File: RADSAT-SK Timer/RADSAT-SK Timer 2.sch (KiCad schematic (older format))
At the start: 52 parts, among them J201 Conn_01x07, J202 Conn_01x05, J203 Conn_01x03, J204 Conn_01x02, J205 Conn_01x02, J206 Conn_01x02, J210 ZX62WRD-B-5PC, Q201 IRLML2060, Q202 IRLML2060, Q204 IRLML2060, Q205 IRLML2060, Q206 IRLML2060, SW201 SW_Push, SW202 SW_Push, SW203 SW_Push, SW204 SW_Push, SW205 SW_Push, SW206 SW_Push, U202 LTC3440EMSPBF, U230 CPC1117N, U240 CPC1117N, U250 CPC1117N, U260 CPC1117N

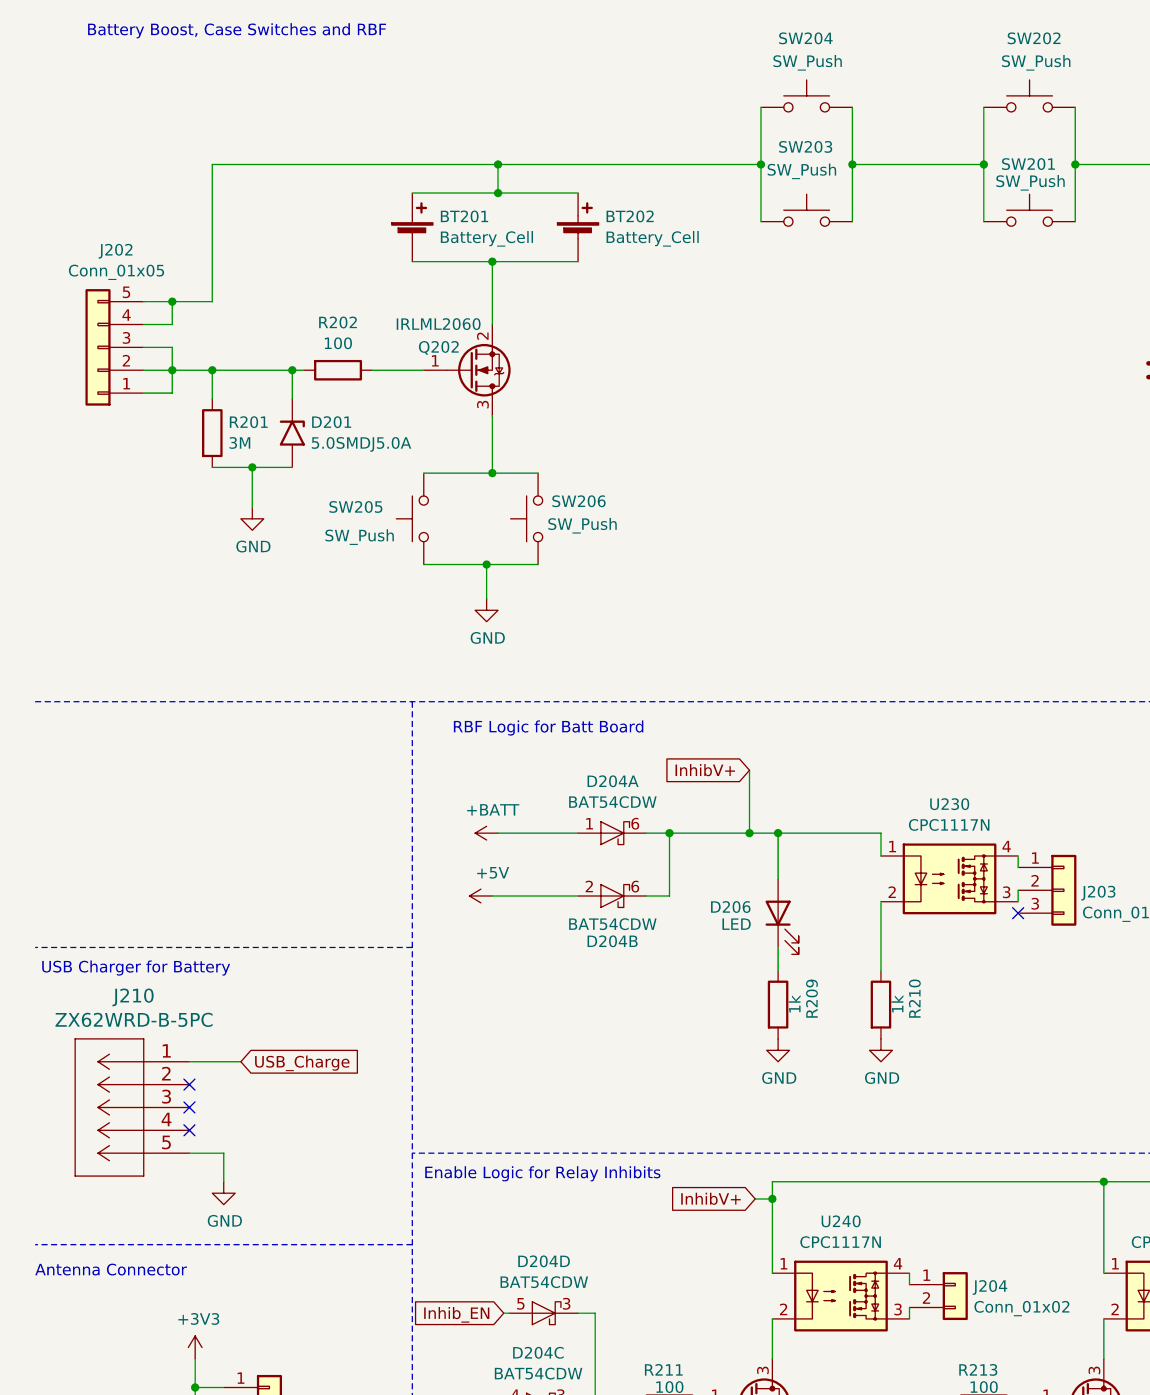
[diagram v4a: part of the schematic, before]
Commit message: Made changes to accomadate the RBF alternate charge plug
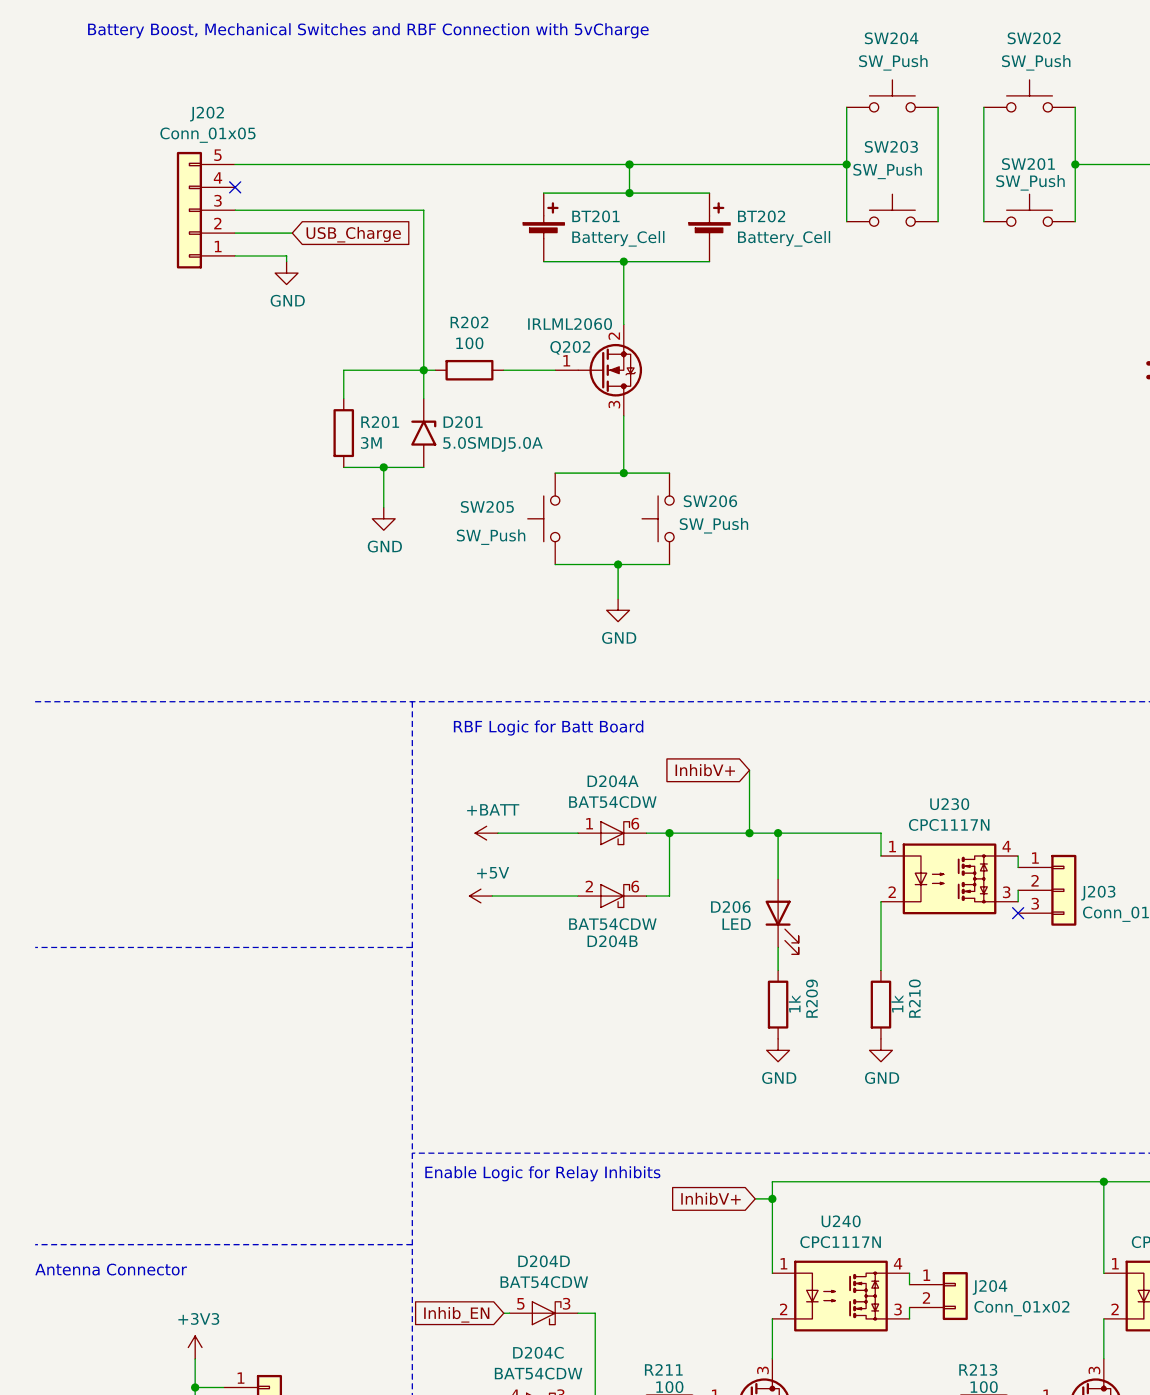
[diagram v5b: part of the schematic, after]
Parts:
- removed J210: ZX62WRD-B-5PC, CONN_ZX62WRD-B-5PC_HIR:CONN_ZX62WRD-B-5PC_HIR, symbol CONN_ZX62WRD-B-5PC_HIR:ZX62WRD-B-5PC
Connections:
- net GND: now also J202.1 (Pin_1)
- net USB_Charge: now also J202.2 (Pin_2)
- net at BT201.1 (+), BT202.1 (+), J202.5 (Pin_5)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: no longer J202.4 (Pin_4)
- net at SW203.2, SW204.2: no longer SW201.1, SW202.1
- net at D201.1 (A1), J202.3 (Pin_3), R201.1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: no longer J202.1 (Pin_1), J202.2 (Pin_2)
- new net: SW201.1, SW202.1
- no-connect marks 5 -> 3
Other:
- note added: "Battery Boost, Mechanical Switches and RBF Connection with 5vCharge"
- note removed: "Battery Boost, Case Switches and RBF"
- note removed: "USB Charger for Battery"
- moved on the sheet: BT201, BT202, D201, J202, Q202, R201, R202, SW203, SW204, SW205, SW206

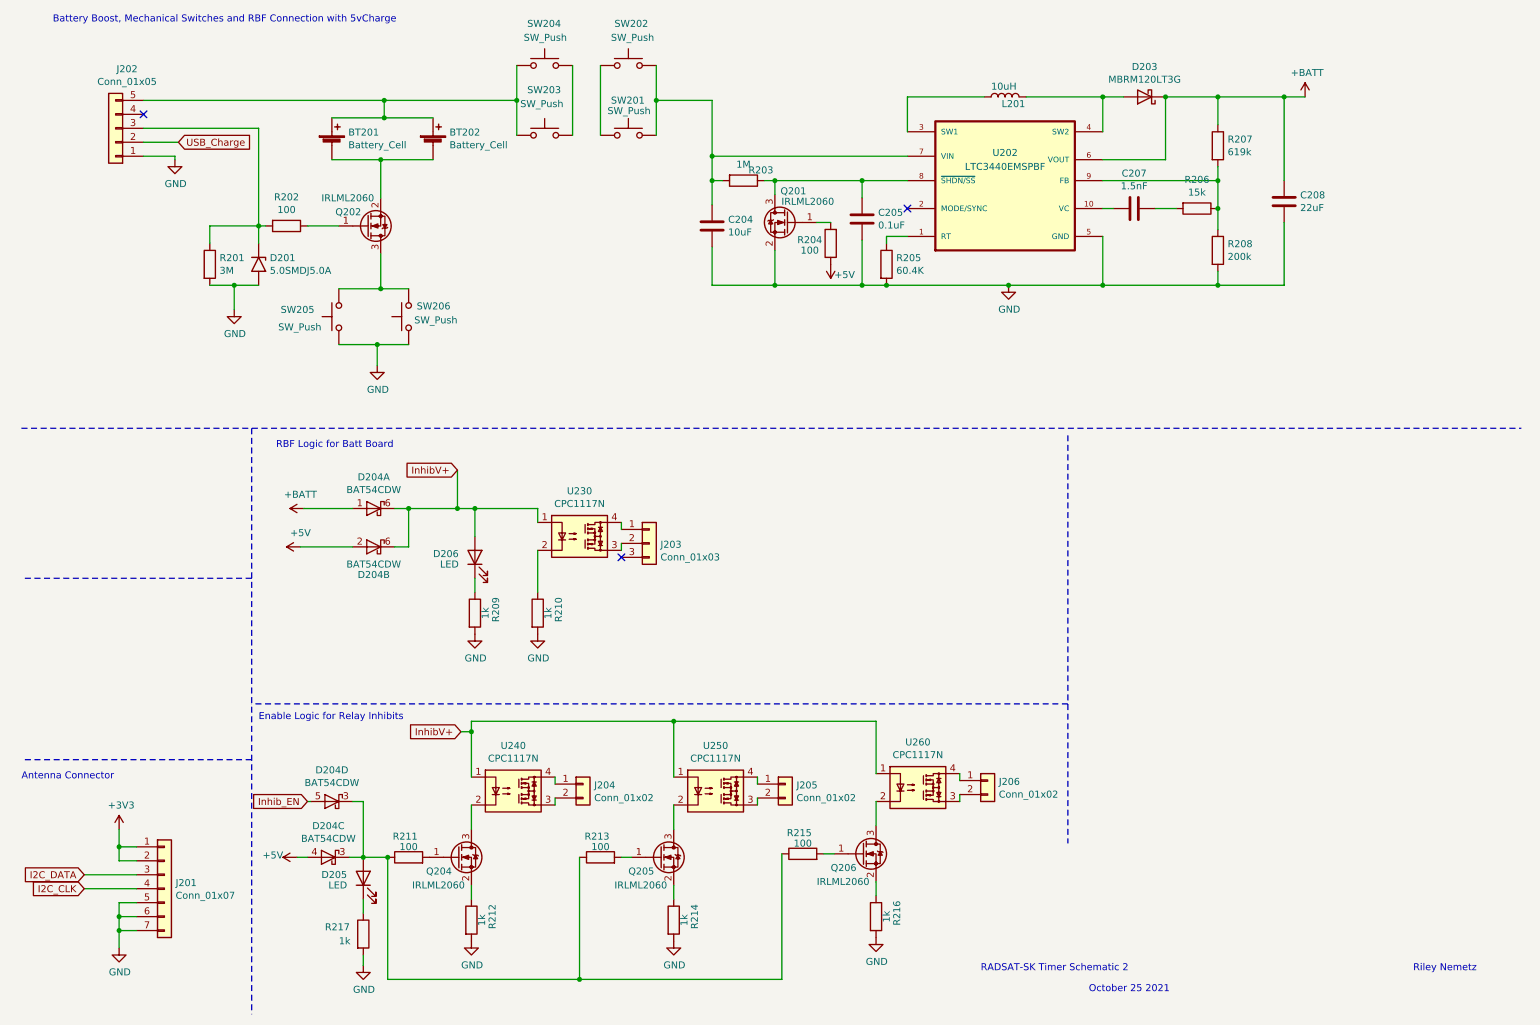
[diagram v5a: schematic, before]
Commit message: RBF Circuit was modified and new components added to BOM
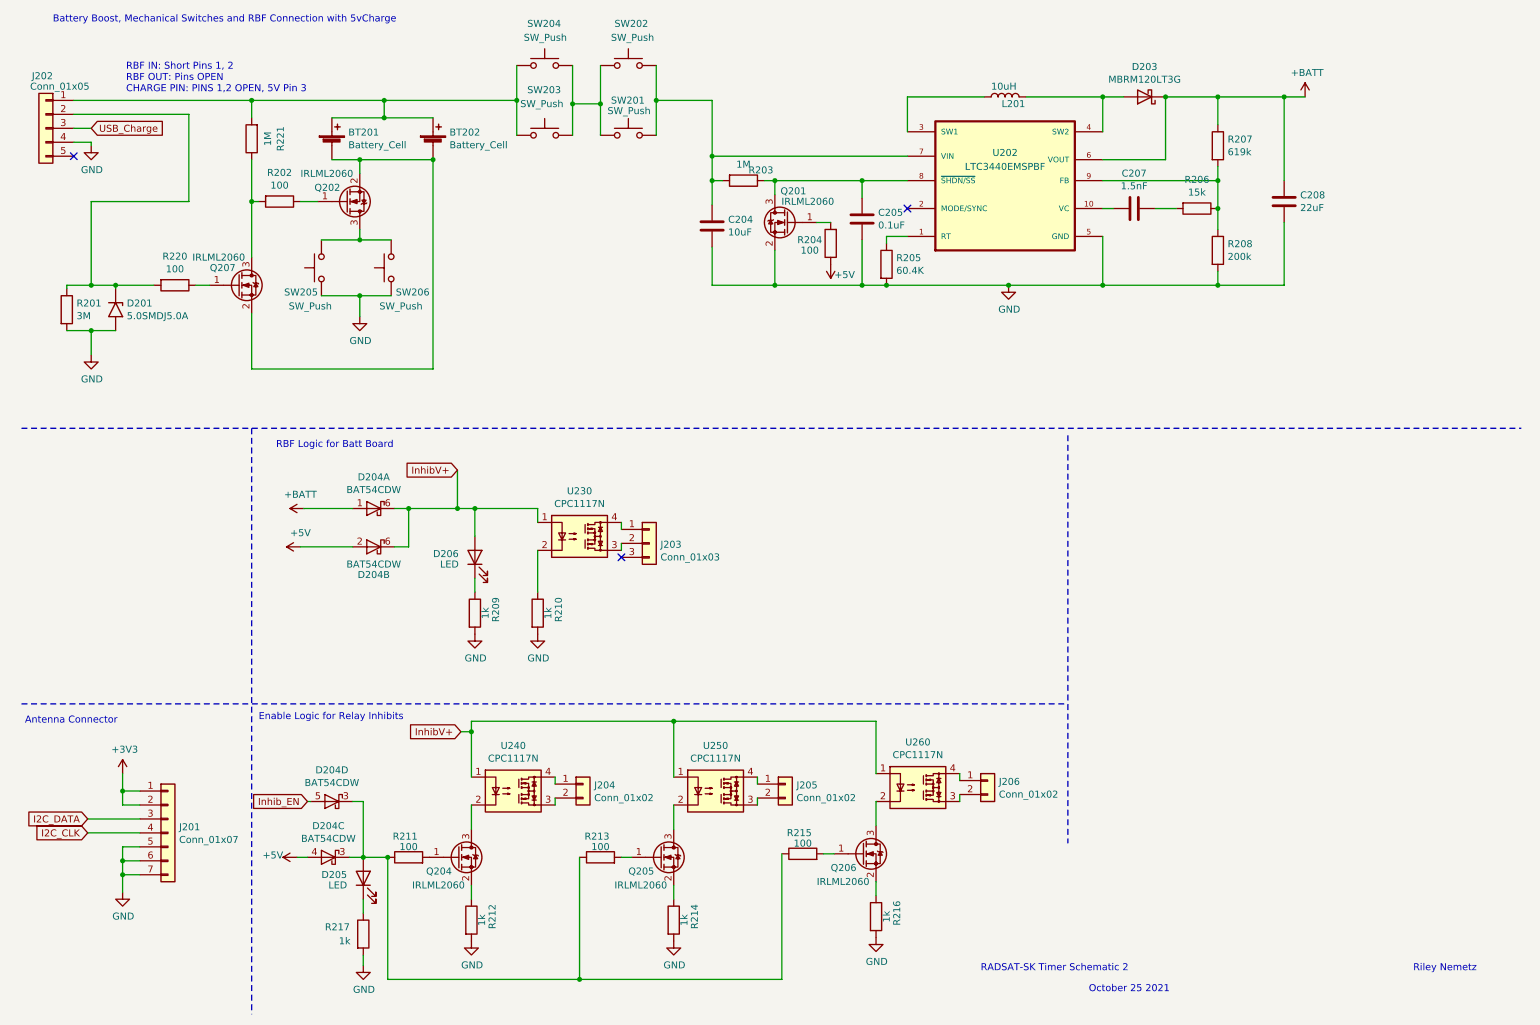
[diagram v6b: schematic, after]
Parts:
- added Q207: IRLML2060, Package_TO_SOT_SMD:SOT-23_Handsoldering, symbol Transistor_FET:IRLML2060
- added R220: 100, Resistor_SMD:R_0805_2012Metric, symbol Device:R
- added R221: 1M, Resistor_SMD:R_0805_2012Metric, symbol Device:R
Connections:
- net GND: now also J202.4 (Pin_4); no longer J202.1 (Pin_1)
- net USB_Charge: now also J202.3 (Pin_3); no longer J202.2 (Pin_2)
- net at BT201.1 (+), BT202.1 (+), SW203.1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: now also J202.1 (Pin_1), R221.2; no longer J202.5 (Pin_5)
- net at BT201.2 (-), BT202.2 (-), Q202.2 (S): now also Q207.2 (S)
- net at SW203.2, SW204.2: now also SW201.1, SW202.1
- net at D201.1 (A1), R201.1: now also J202.2 (Pin_2), R220.2; no longer J202.3 (Pin_3), R202.2
- new net: Q207.3 (D), R202.2, R221.1
- new net: Q207.1 (G), R220.1
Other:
- note added: "RBF IN: Short Pins 1, 2\nRBF OUT: Pins OPEN\nCHARGE PIN: PINS 1,2 OPEN, 5V Pin 3"
- moved on the sheet: D201, J201, J202, Q202, R201, R202, SW205, SW206

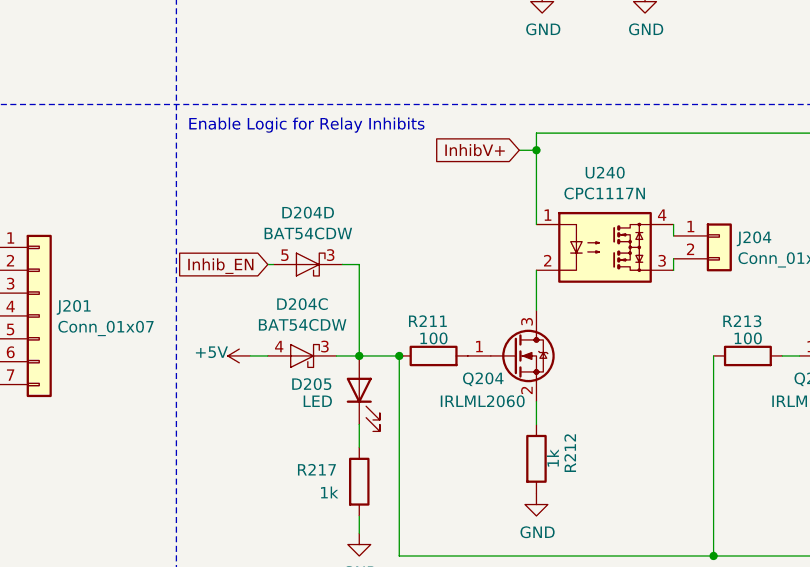
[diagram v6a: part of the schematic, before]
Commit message: Layout ios near complete just need to make custom inductor footprint
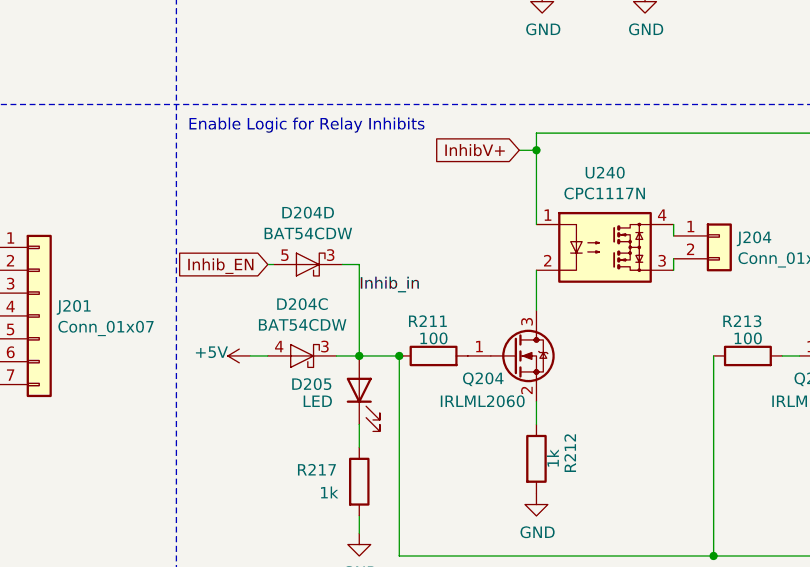
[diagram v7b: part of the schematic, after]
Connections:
- net Inhib_in: now reaches D204.3 (K), D204.3 (K), D205.2 (A), R211.1, R213.1, R215.1
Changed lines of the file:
@@
 Wire Wire Line
 	4625 1275 4625 1500
+Text Label 2925 6400 0    50   ~ 0
+Inhib_in
 $EndSCHEMATC

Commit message: Modified Inductor Footprint, fixed 3d Model orientation, generated gerbers and drill files. Still unsure about ESD Protection, but can simply remove components from board later.
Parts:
- L201: footprint Inductor_SMD:L_0805_2012Metric -> Sumida_inductor:Sumida_inductor
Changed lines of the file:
@@
 F 0 "L201" V 7475 1250 50  0000 R CNN
 F 1 "10uH" V 7600 1325 50  0000 R CNN
-F 2 "Inductor_SMD:L_0805_2012Metric" H 7525 1225 50  0001 C CNN
+F 2 "Sumida_inductor:Sumida_inductor" H 7525 1225 50  0001 C CNN
 F 3 "~" H 7525 1225 50  0001 C CNN
 	1    7525 1225
